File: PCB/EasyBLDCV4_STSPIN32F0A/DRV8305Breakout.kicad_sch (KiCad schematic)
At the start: 29 parts, among them Q1 IAUC60N04S6N031HATMA1, Q2 IAUC60N04S6N031HATMA1, Q3 IAUC60N04S6N031HATMA1, U2 INA180A1IDBVR

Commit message: Finished Schematic Assigned Footprints
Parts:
- C10: renamed from C6; footprint (none) -> Capacitor_SMD:C_1206_3216Metric
- C11: renamed from C7; footprint (none) -> Capacitor_SMD:C_1206_3216Metric
- C4: renamed from C9; footprint (none) -> Capacitor_SMD:C_0402_1005Metric
- C5: renamed from C10; footprint (none) -> Capacitor_SMD:C_0402_1005Metric
- C6: renamed from C8; footprint (none) -> Capacitor_SMD:C_1206_3216Metric
- C7: renamed from C3; footprint (none) -> Capacitor_SMD:C_1206_3216Metric
- C8: renamed from C4; footprint (none) -> Capacitor_SMD:C_1206_3216Metric
- C9: renamed from C5; footprint (none) -> Capacitor_SMD:C_1206_3216Metric
- Q1, Q2, Q3: footprint PG-TDSON-8-56 -> EasyBLDC:PG-TDSON-8-56
- R1: renamed from R5; footprint (none) -> Resistor_SMD:R_0402_1005Metric
- R10: renamed from R12; footprint (none) -> Resistor_SMD:R_0402_1005Metric
- R11: renamed from R15; footprint (none) -> Resistor_SMD:R_0402_1005Metric
- R12: renamed from R17; footprint (none) -> Resistor_SMD:R_0402_1005Metric
- R13: renamed from R23; footprint (none) -> Resistor_SMD:R_0402_1005Metric
- R14: renamed from R11; footprint (none) -> Resistor_SMD:R_2512_6332Metric
- R15: renamed from R13; footprint (none) -> Resistor_SMD:R_0402_1005Metric
- R16: renamed from R18; footprint (none) -> Resistor_SMD:R_0402_1005Metric
- R17: renamed from R24; footprint (none) -> Resistor_SMD:R_0402_1005Metric
- R2: renamed from R7; footprint (none) -> Resistor_SMD:R_0402_1005Metric
- R3: renamed from R9; footprint (none) -> Resistor_SMD:R_0402_1005Metric
- R4: renamed from R6; footprint (none) -> Resistor_SMD:R_0402_1005Metric
- R5: renamed from R8; footprint (none) -> Resistor_SMD:R_0402_1005Metric
- R6: renamed from R10; footprint (none) -> Resistor_SMD:R_0402_1005Metric
- R7: renamed from R14; footprint (none) -> Resistor_SMD:R_0402_1005Metric
- R8: renamed from R16; footprint (none) -> Resistor_SMD:R_0402_1005Metric
- R9: renamed from R19; footprint (none) -> Resistor_SMD:R_0402_1005Metric
- U1: renamed from U2; footprint DBV0005A_N -> EasyBLDC:DBV0005A_N

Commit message: Started Layout
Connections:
- net BEMF_A: no longer R12.2, R13.2, R16.2, R17.2, R8.1, R9.1
- net MOT_A: no longer R12.1, R13.1
- net MOT_B: now also R12.1
- net MOT_C: now also R13.1
- new net BEMF_B: R12.2, R16.2, R8.1
- new net BEMF_C: R13.2, R17.2, R9.1
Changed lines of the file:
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@@
 		)
 	)
-	(global_label "MOT_A"
+	(global_label "MOT_C"
 		(shape input)
 		(at 107.95 120.65 180)
@@
 		)
 		(property "Intersheetrefs" "${INTERSHEET_REFS}"
-			(at 99.1591 120.65 0)
+			(at 98.9777 120.65 0)
 			(effects
 				(font
@@
 		)
 	)
-	(global_label "MOT_A"
+	(global_label "MOT_B"
 		(shape input)
 		(at 72.39 120.65 180)
@@
 		)
 		(property "Intersheetrefs" "${INTERSHEET_REFS}"
-			(at 63.5991 120.65 0)
+			(at 63.4177 120.65 0)
 			(effects
 				(font
@@
 		)
 	)
-	(global_label "BEMF_A"
+	(global_label "BEMF_B"
 		(shape output)
 		(at 88.9 125.73 0)
@@
 		)
 		(property "Intersheetrefs" "${INTERSHEET_REFS}"
-			(at 98.9004 125.73 0)
+			(at 99.0818 125.73 0)
 			(effects
 				(font
@@
 		)
 	)
-	(global_label "BEMF_A"
+	(global_label "BEMF_C"
 		(shape output)
 		(at 124.46 125.73 0)
@@
 		)
 		(property "Intersheetrefs" "${INTERSHEET_REFS}"
-			(at 134.4604 125.73 0)
+			(at 134.6418 125.73 0)
 			(effects
 				(font

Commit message: Fixed DRC Errors. Ready for review
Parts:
- Q1, Q2, Q3: footprint EasyBLDC:PG-TDSON-8-56 -> EasyBLDC:PG-TDSON-8-56-2
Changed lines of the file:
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@@
 			)
 		)
-		(property "Footprint" "EasyBLDC:PG-TDSON-8-56"
+		(property "Footprint" "EasyBLDC:PG-TDSON-8-56-2"
 			(at 92.71 49.53 0)
 			(effects
@@
 			)
 		)
-		(property "Footprint" "EasyBLDC:PG-TDSON-8-56"
+		(property "Footprint" "EasyBLDC:PG-TDSON-8-56-2"
 			(at 241.3 49.53 0)
 			(effects
@@
 			)
 		)
-		(property "Footprint" "EasyBLDC:PG-TDSON-8-56"
+		(property "Footprint" "EasyBLDC:PG-TDSON-8-56-2"
 			(at 166.37 49.53 0)
 			(effects

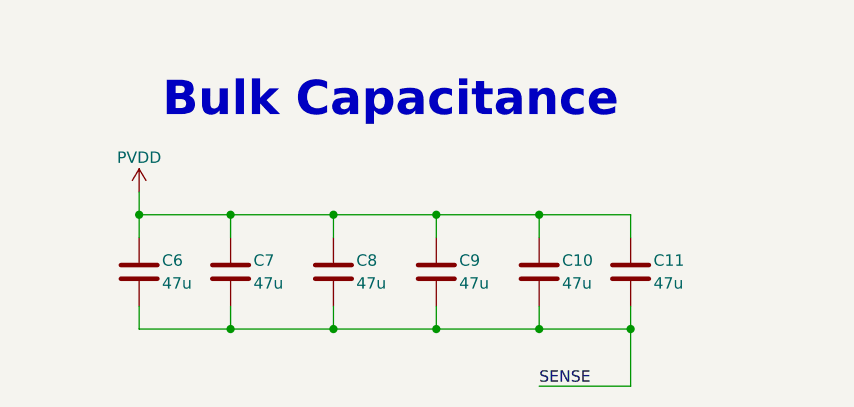
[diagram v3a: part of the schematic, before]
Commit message: Changed out 0201 resistors, production version
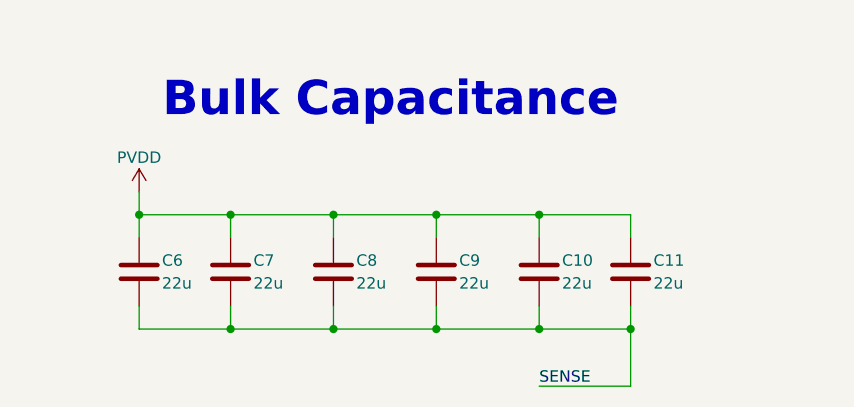
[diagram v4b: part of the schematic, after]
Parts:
- C10, C11, C6, C7, C8, C9: value 47u -> 22u
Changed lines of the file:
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@@
 			)
 		)
-		(property "Value" "47u"
+		(property "Value" "22u"
 			(at 83.82 176.53 0)
 			(effects
@@
 			)
 		)
-		(property "Value" "47u"
+		(property "Value" "22u"
 			(at 95.25 176.53 0)
 			(effects
@@
 			)
 		)
-		(property "Value" "47u"
+		(property "Value" "22u"
 			(at 72.39 176.53 0)
 			(effects
@@
 			)
 		)
-		(property "Value" "47u"
+		(property "Value" "22u"
 			(at 116.84 176.53 0)
 			(effects
@@
 			)
 		)
-		(property "Value" "47u"
+		(property "Value" "22u"
 			(at 62.23 176.53 0)
 			(effects
@@
 			)
 		)
-		(property "Value" "47u"
+		(property "Value" "22u"
 			(at 106.68 176.53 0)
 			(effects
